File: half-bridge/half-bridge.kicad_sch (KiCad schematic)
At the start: 111 parts, among them J1 Conn_01x11_Pin, J2 MountingHole_Pad, J3 Conn_01x11_Pin, J4 Conn_01x11_Pin, J5 Conn_01x11_Pin, J6 Conn_01x11_Pin, J7 MountingHole_Pad, J8 MountingHole_Pad, J9 MountingHole_Pad, Q1 EPC2306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

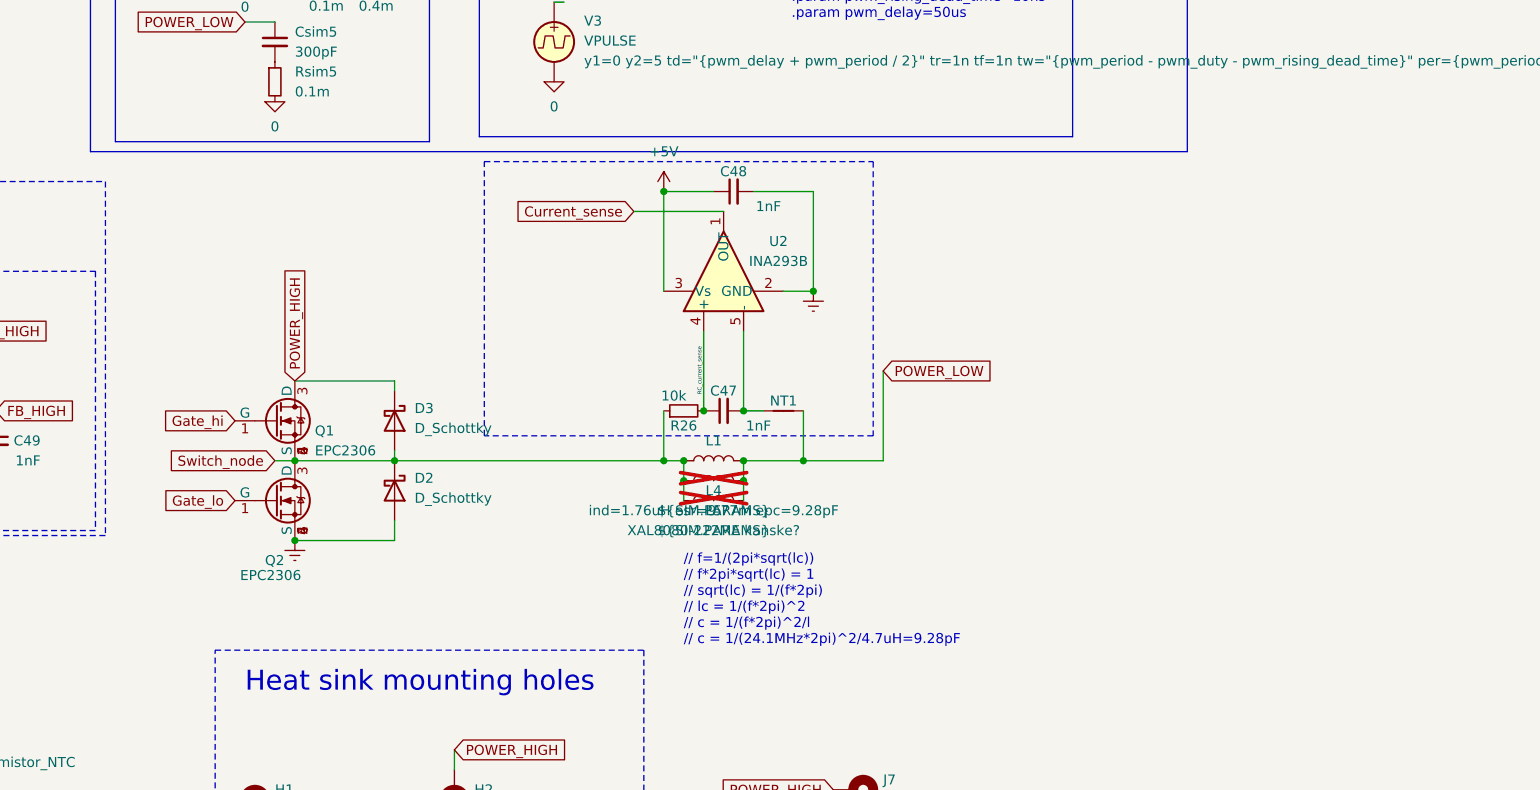
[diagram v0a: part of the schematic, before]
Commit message: Add current sense resistors
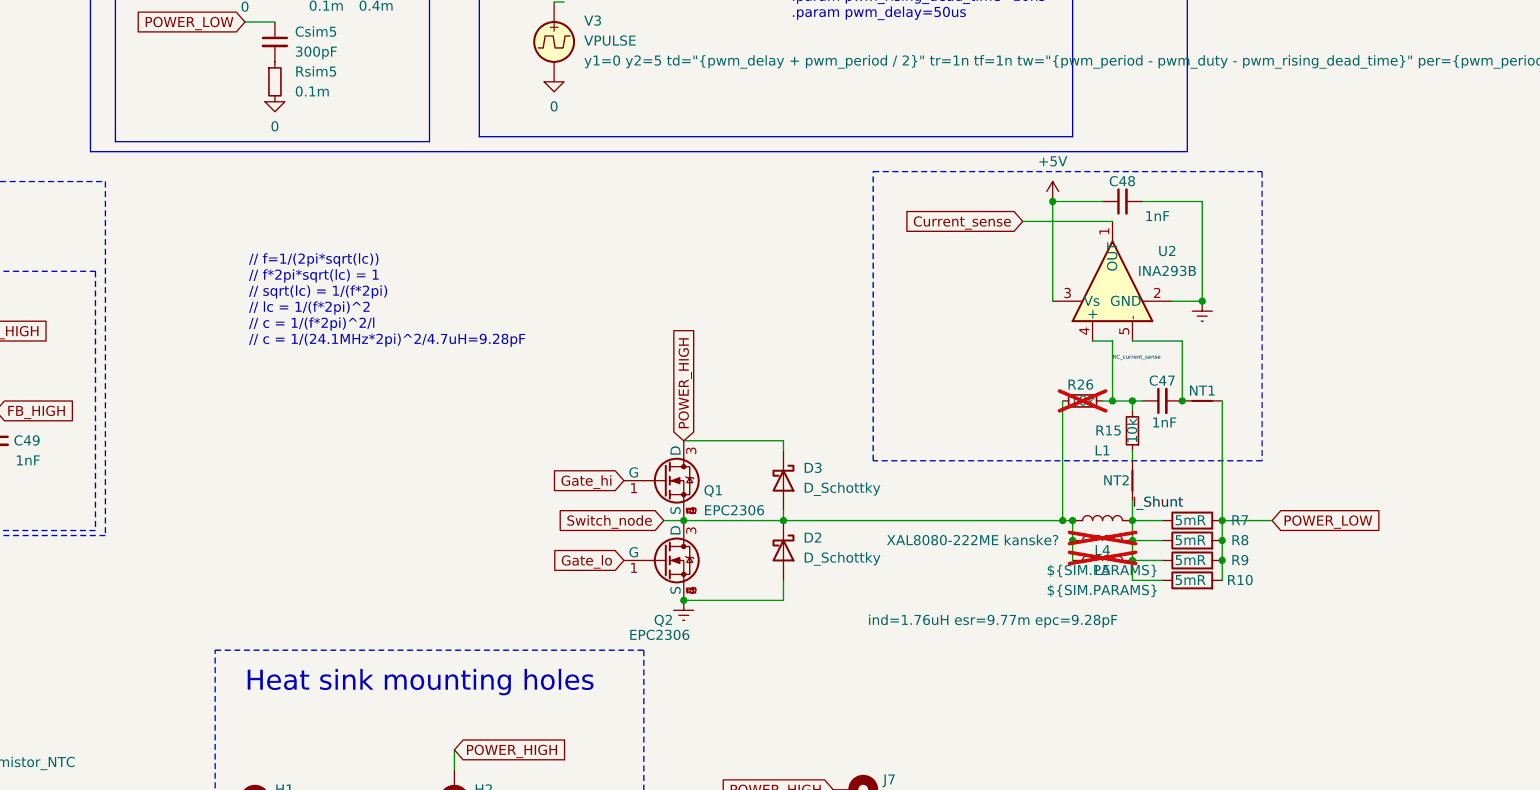
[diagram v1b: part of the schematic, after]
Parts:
- added NT2: NetTie_2, NetTie:NetTie-2_SMD_Pad0.5mm, symbol Device:NetTie_2
- added R10, R7, R8, R9: 5mR, Library:R_0508_1220Metric, symbol Device:R
- added R15: 10k, Resistor_SMD:R_0603_1608Metric, symbol Device:R_Small
- R26: footprint Resistor_SMD:R_1206_3216Metric -> Resistor_SMD:R_0603_1608Metric; now not fitted
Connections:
- net POWER_LOW: now also R10.2, R7.2, R8.2, R9.2; no longer L1.2, L4.2, L5.2
- net RC_current_sense: now also R15.2
- new net: NT2.1, R15.1
- new net I_Shunt: L1.2, L4.2, L5.2, NT2.2, R10.1, R7.1, R8.1, R9.1
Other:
- moved on the sheet: C47, C48, D2, D3, L1, L4, L5, NT1, Q1, Q2, U2

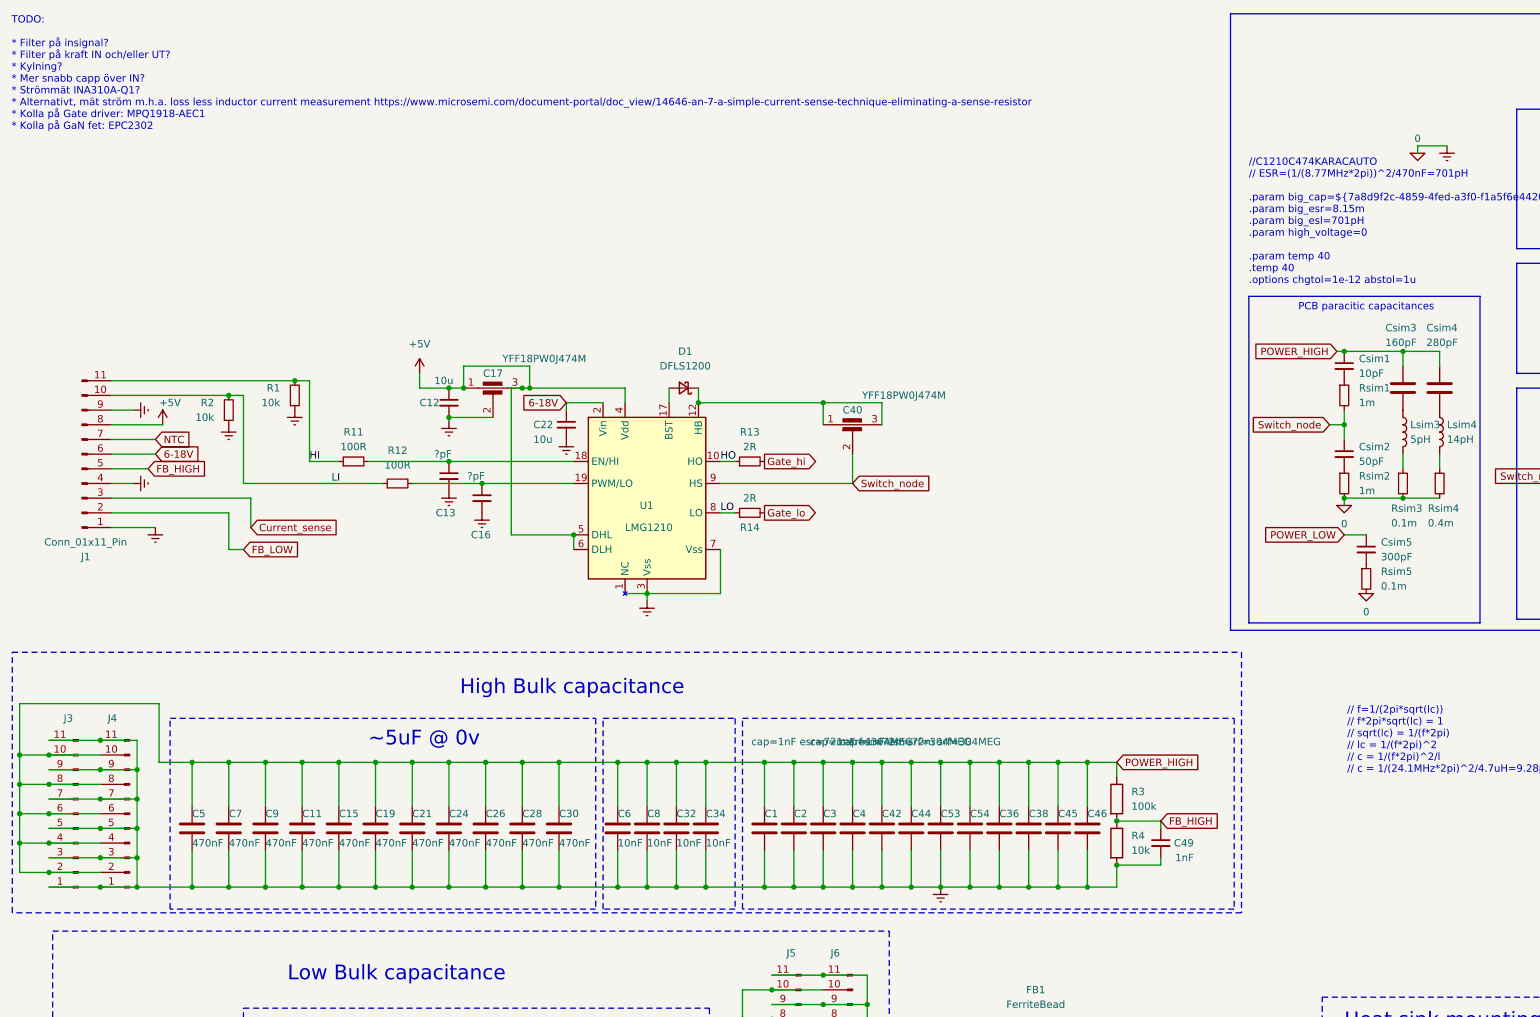
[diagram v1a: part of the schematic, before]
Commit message: Cleanup most DRC errors
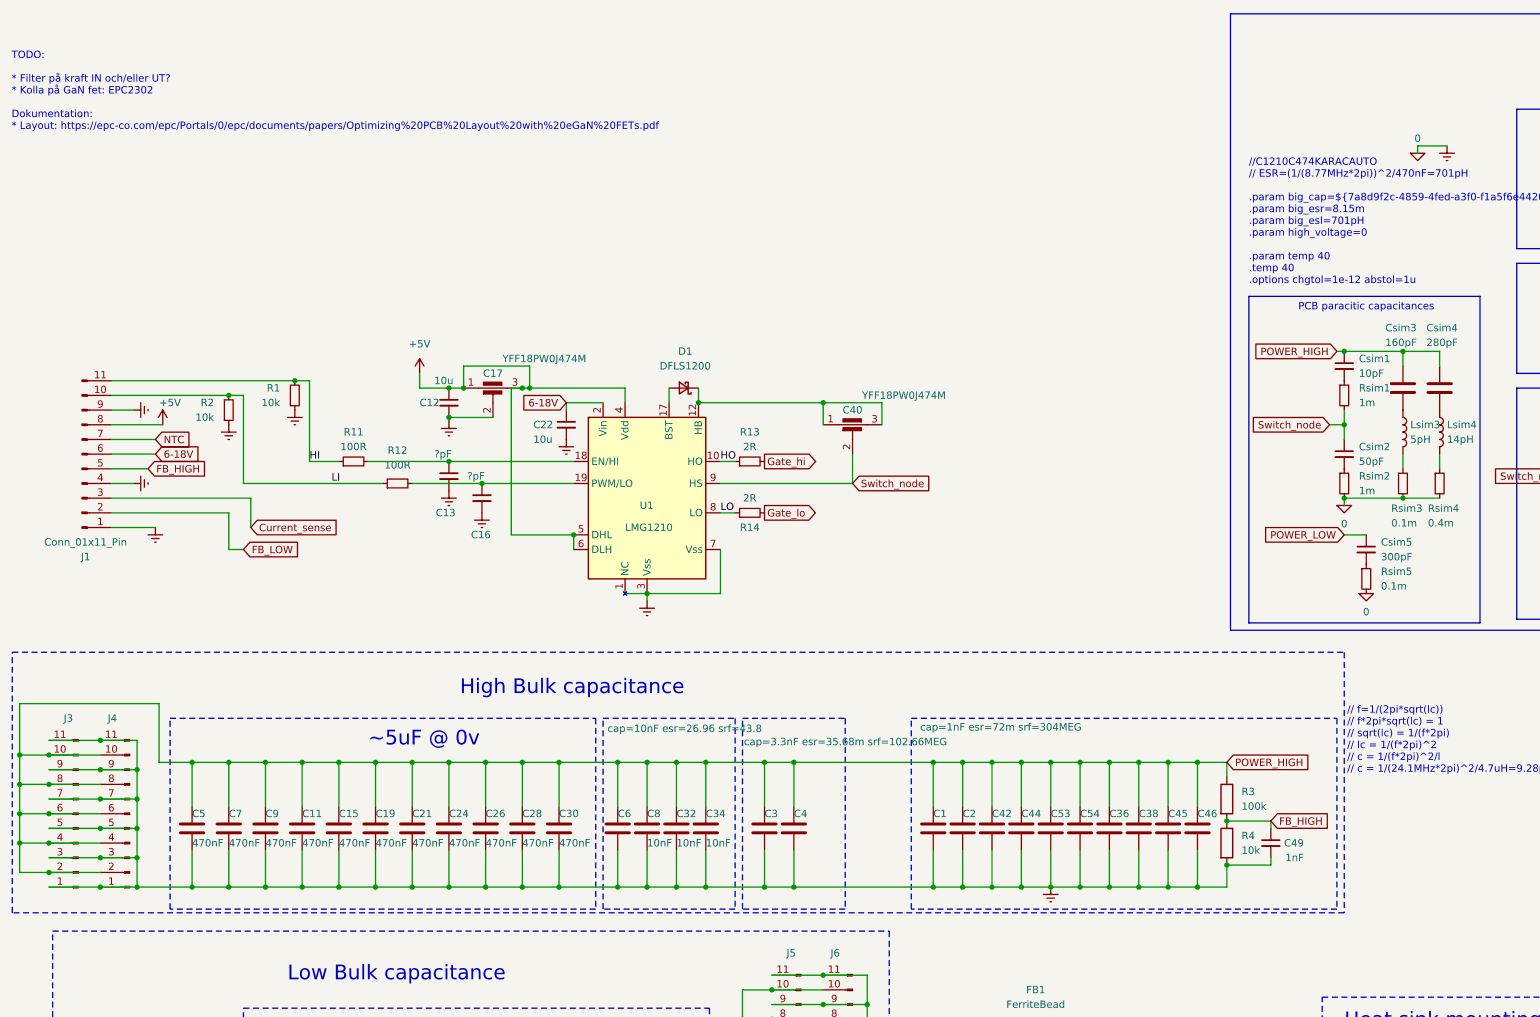
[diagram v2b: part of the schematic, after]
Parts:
- C3, C4: footprint Capacitor_SMD:C_0402_1005Metric -> Capacitor_SMD:C_0603_1608Metric
- C6: value 10nF -> ${SIM.PARAMS}
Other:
- note added: "TODO: * Filter på kraft IN och/eller UT? * Kolla på GaN fet: EPC2302 Dokumentation: * Layout: https://epc-co.com/epc/Portals/0/epc/documents/papers/Optimizing%20PCB%20Layout%20with%20eGaN%20FETs.pdf"
- note removed: "TODO: * Filter på insignal? * Filter på kraft IN och/eller UT? * Kylning? * Mer snabb capp över IN? * Strömmät INA310A-Q1? * Alternativt, mät ström m.h.a. loss less inductor current measurement https://www.microsemi.com/document-portal/doc_view/14646-an-7-a-simple-current-sense-technique-eliminating-a-sense-resistor * Kolla på Gate driver: MPQ1918-AEC1 * Kolla på GaN fet: EPC2302"
- moved on the sheet: C1, C2, C3, C36, C38, C4, C42, C44, C45, C46, C49, C53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

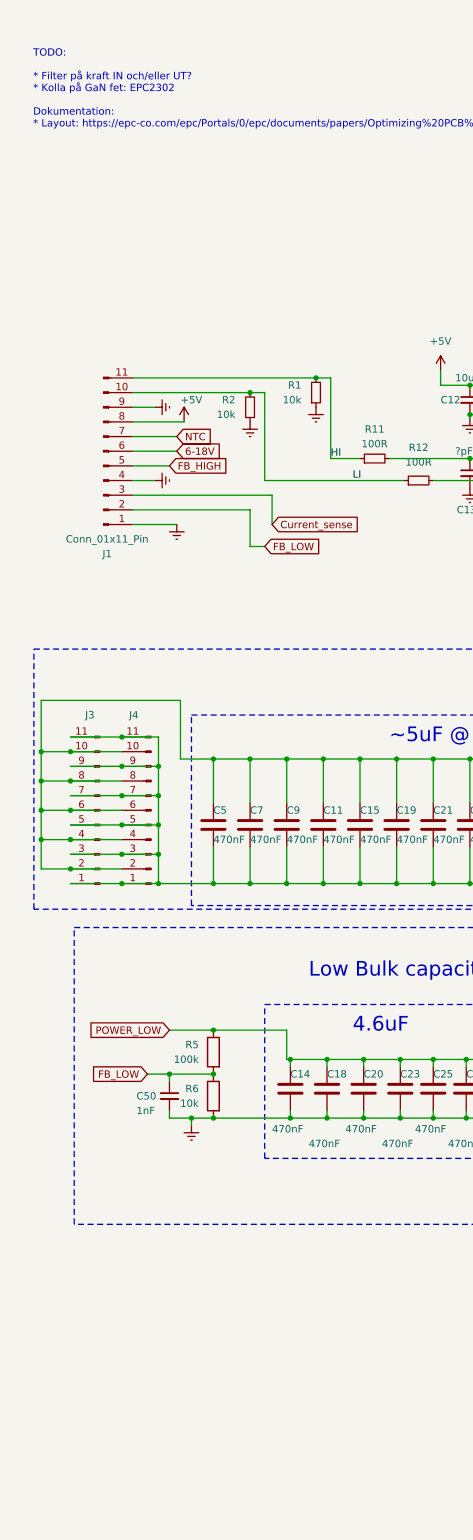
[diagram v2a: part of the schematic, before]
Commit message: Increase POWER_HIGH area further
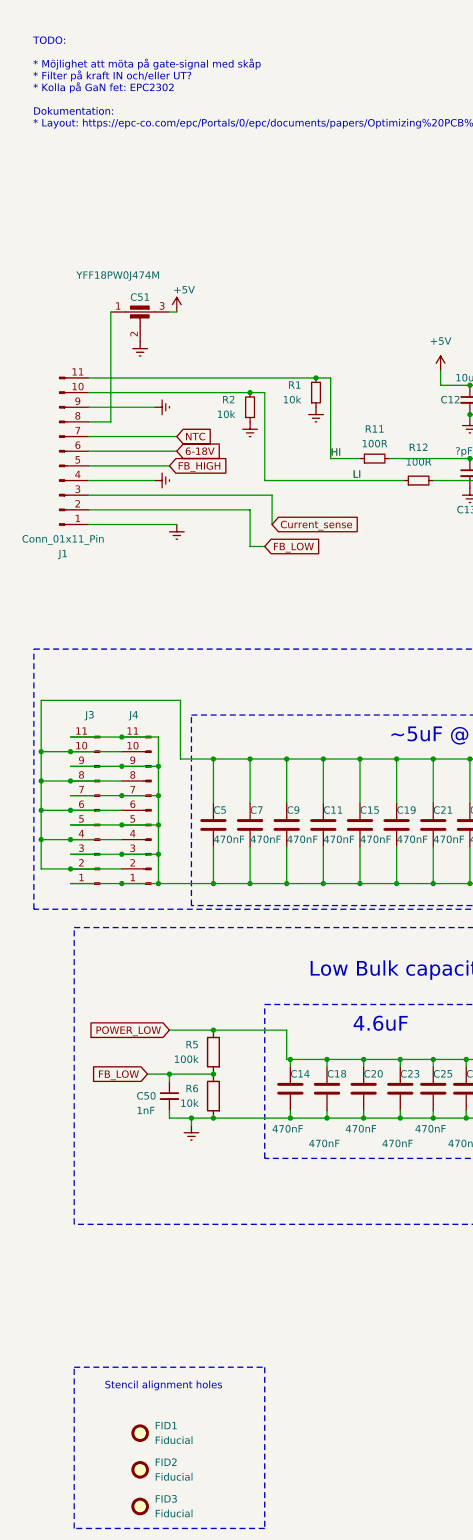
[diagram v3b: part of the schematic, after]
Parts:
- added C51: YFF18PW0J474M, Library:C_0603_1608Metric_Feedthrough_W_Vias, symbol Device:C_Feedthrough
- added FID1, FID2, FID3: Fiducial, TestPoint:TestPoint_Pad_D1.0mm, symbol Mechanical:Fiducial
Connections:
- net +5V: now also C51.3; no longer J1.8 (Pin_8)
- net 0: now also C51.2
- new net: C51.1, J1.8 (Pin_8)
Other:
- note added: "Stencil alignment holes"
- note added: "TODO: * Möjlighet att möta på gate-signal med skåp * Filter på kraft IN och/eller UT? * Kolla på GaN fet: EPC2302 Dokumentation: * Layout: https://epc-co.com/epc/Portals/0/epc/documents/papers/Optimizing%20PCB%20Layout%20with%20eGaN%20FETs.pdf"
- note removed: "TODO: * Filter på kraft IN och/eller UT? * Kolla på GaN fet: EPC2302 Dokumentation: * Layout: https://epc-co.com/epc/Portals/0/epc/documents/papers/Optimizing%20PCB%20Layout%20with%20eGaN%20FETs.pdf"
- moved on the sheet: J1

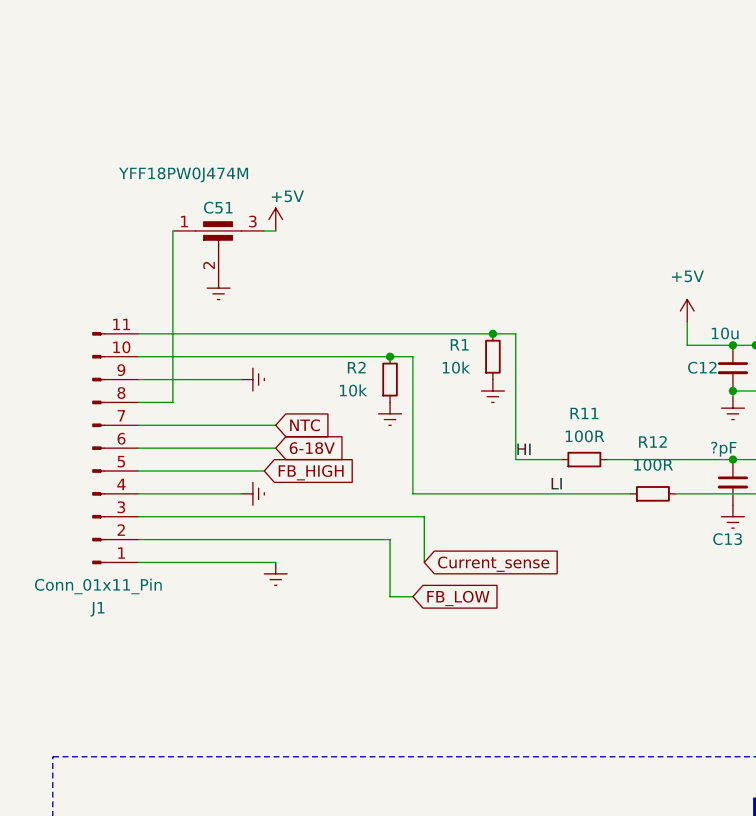
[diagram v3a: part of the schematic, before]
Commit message: Change pinout and add voltage regulators to controller
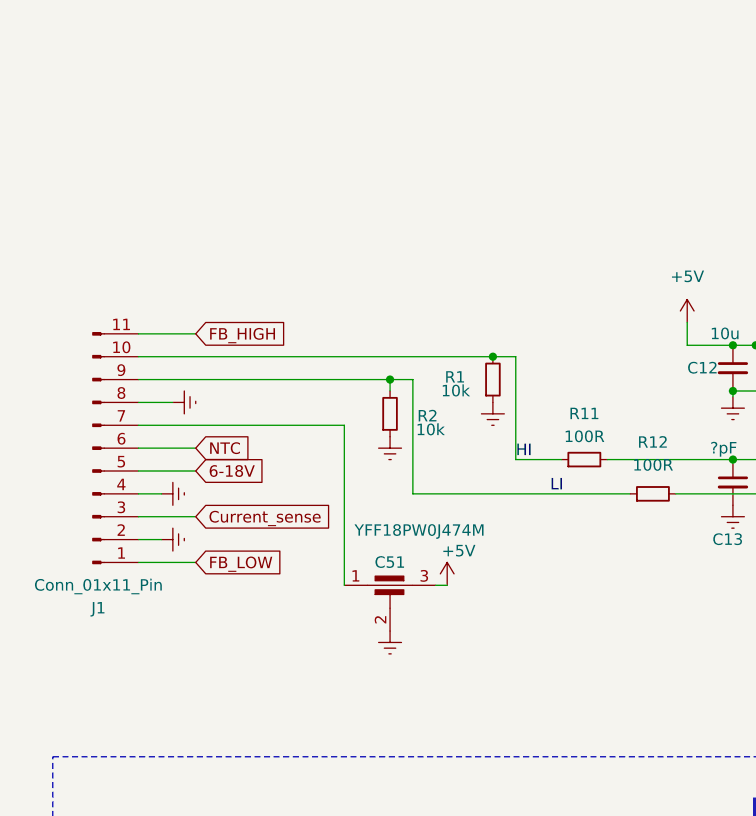
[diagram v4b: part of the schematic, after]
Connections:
- net 0: now also J1.2 (Pin_2), J1.8 (Pin_8); no longer J1.1 (Pin_1), J1.9 (Pin_9)
- net 6-18V: now also J1.5 (Pin_5); no longer J1.6 (Pin_6)
- net FB_HIGH: now also J1.11 (Pin_11); no longer J1.5 (Pin_5)
- net FB_LOW: now also J1.1 (Pin_1); no longer J1.2 (Pin_2)
- net HI: now also J1.10 (Pin_10); no longer J1.11 (Pin_11)
- net LI: now also J1.9 (Pin_9); no longer J1.10 (Pin_10)
- net NTC: now also J1.6 (Pin_6); no longer J1.7 (Pin_7)
- net at C51.1: now also J1.7 (Pin_7); no longer J1.8 (Pin_8)
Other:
- moved on the sheet: C51, R1, R2
